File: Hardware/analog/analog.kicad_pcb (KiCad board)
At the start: 4 copper layers, 128 x 182 mm, 164 parts, among them J201 Würth 74651194R, J202 Würth 74651194R, J301 Conn_02x10_Odd_Even, J501 Conn_01x01, J502 Conn_01x01, J801 Conn_01x02, K801 EA2-3T, M501 Fan_4pin, Q201 IXTH80N075L2, Q202 IXTH80N075L2, Q501 MMBT3904, U201 ADA4522-2, U202 LM431SC, U203 LMT86LMT, U204 ADA4522-2, U205 LM431SC, U206 LMT86LMT, U301 ADUM131D, U302 ADUM131D, U303 ADUM1250, U304 74LVC1G139, U305 AT24CS32-SSHM, U306 FODM217B, U401 ICL7660, U402 MCP1804x-C002xMB, U403 MCP1703AT-5002E/DB, U404 XC6203E33, U405 LP5907MFX-3.3, U501 EMC2101-R, U601 MCP3562, U602 MAX6166, U603 DAC8562, U605 MCP3561, U701 Si5351A-B-GT, U801 PCA9536D, U802 OPA277, U803 MMBT3904, U804 MMBT3904, Y701 25MHz

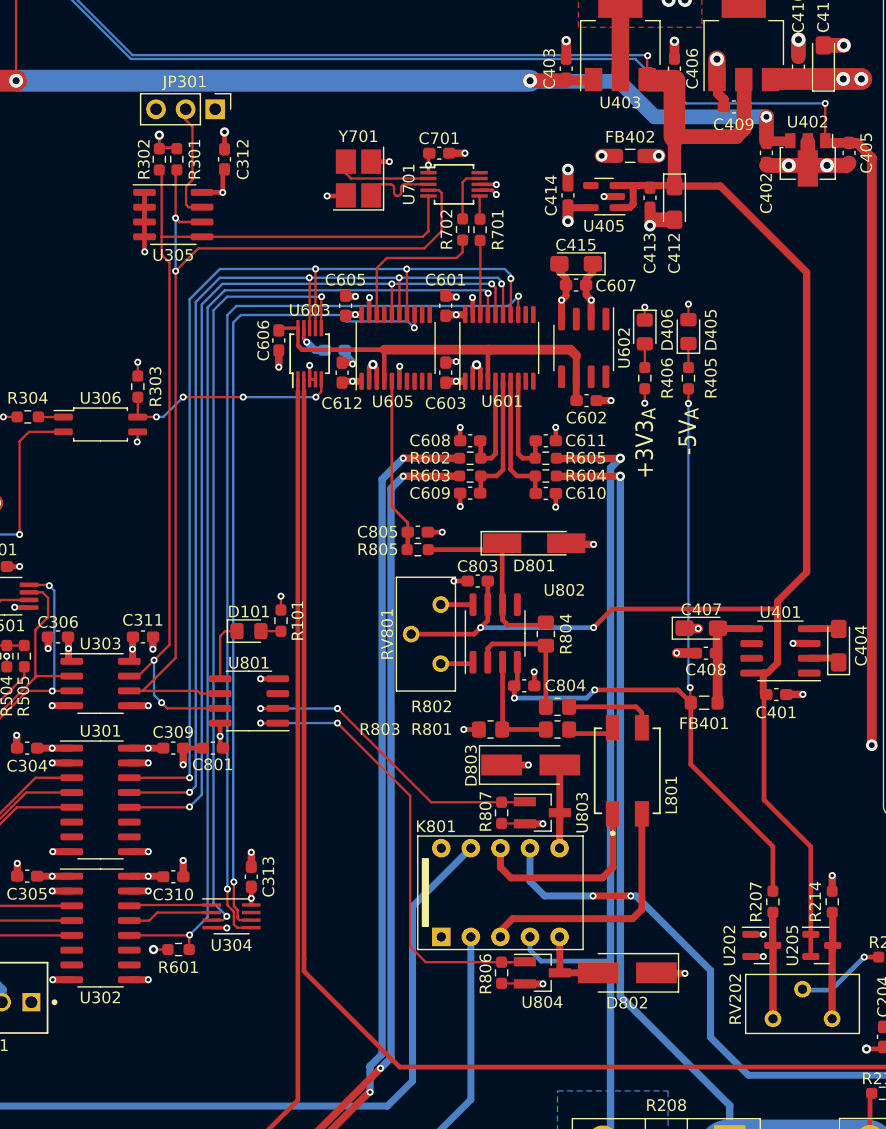
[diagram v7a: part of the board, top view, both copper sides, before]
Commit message: Analog board changes
- Switched IDPROM for a TSSOP-8 package, rather than the SOIC-8 which is
  basically unobtanium

- Minor layout unrelated tweaks
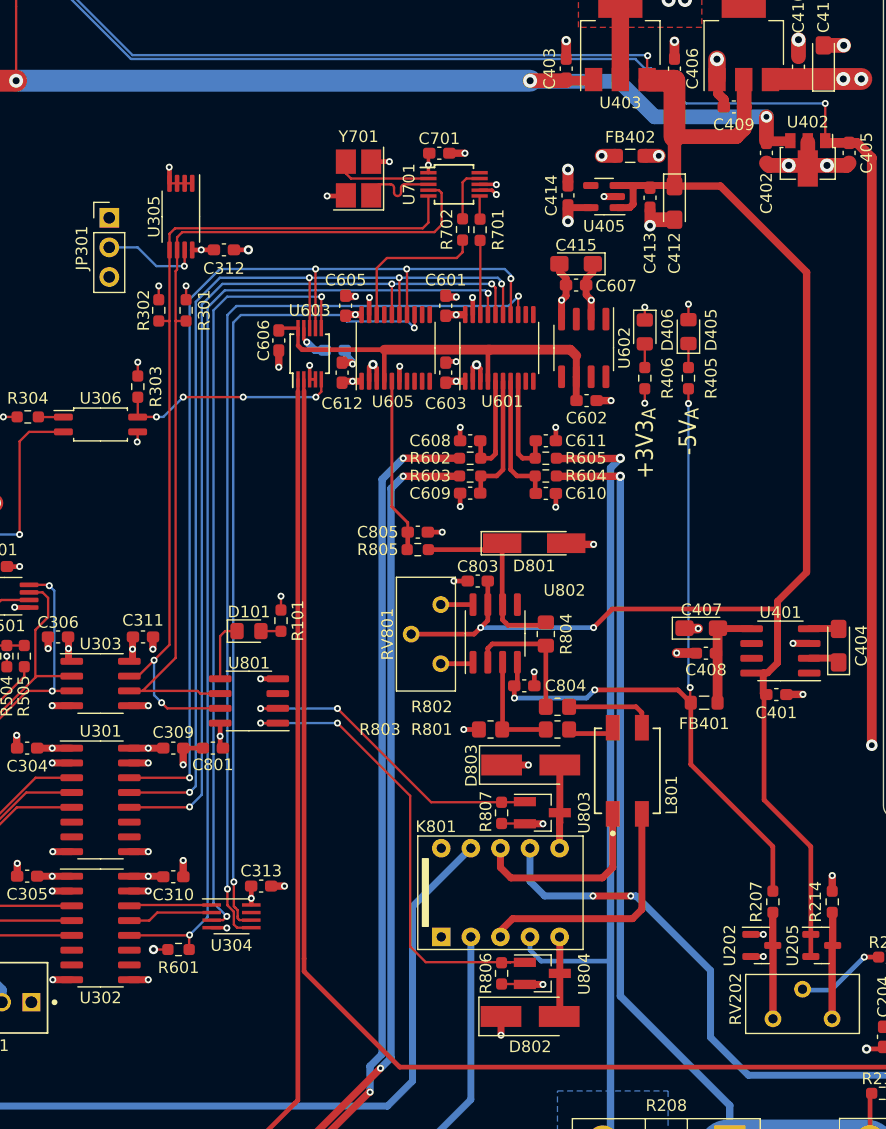
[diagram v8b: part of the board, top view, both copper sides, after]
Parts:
- U305: footprint Package_SO:SOIC-8_3.9x4.9mm_P1.27mm -> Package_SO:TSSOP-8_4.4x3mm_P0.65mm
- moved JP301 13.0 mm to (49.5, 58.5), turned to 0 degrees
- moved R301 13.0 mm to (56.1, 66.5)
- moved R302 13.0 mm to (53.8, 66.5)
- moved D802 9.15 mm to (85.7, 127.1), turned to 0 degrees
- moved C312 7.78 mm to (59.4, 61.2), turned to 0 degrees
- moved C313 1.17 mm to (62.5, 115.9), turned to 0 degrees
- moved U305 0.67 mm to (55.6, 58.4), turned to -90 degrees
- moved R806 0.05 mm to (83.2, 123.4)
- moved U804 0.05 mm to (86.7, 123.4)
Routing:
- net /I2C_SCL: track 87.0 -> 76.0 mm, vias 2 -> 0
- net /I2C_SDA: track 80.8 -> 74.9 mm
- net +3V3: track 40.9 -> 37.7 mm, vias 19 -> 20
- net GND: track 115.1 -> 113.1 mm
- net Net-(JP301-C): track 10.1 -> 8.51 mm, vias 0 -> 1
